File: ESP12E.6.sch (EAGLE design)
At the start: 63 parts, among them CN2 1X4-BIG, J1 1X2-3.5MM, J4 1X2-3.5MM, U1 A5984

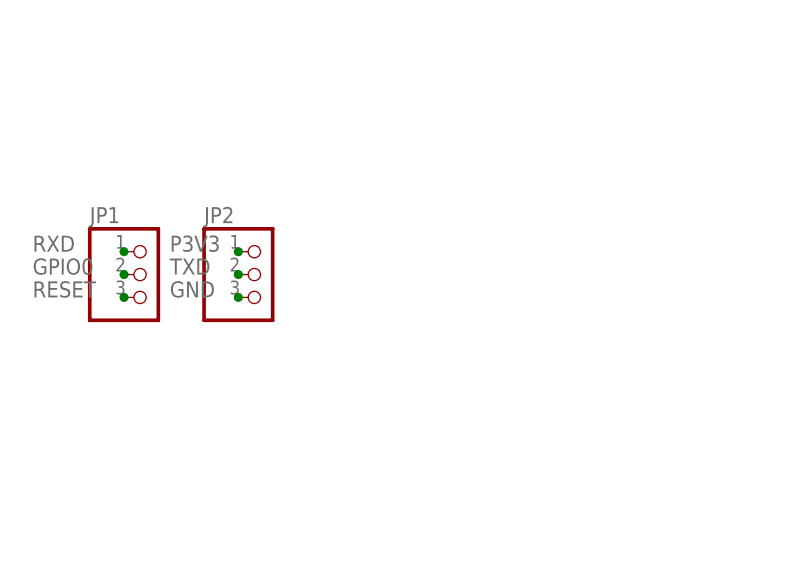
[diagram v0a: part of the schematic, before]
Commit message: //Lowered power via hole sizes to 18 AWG // Added ADC pin exposure
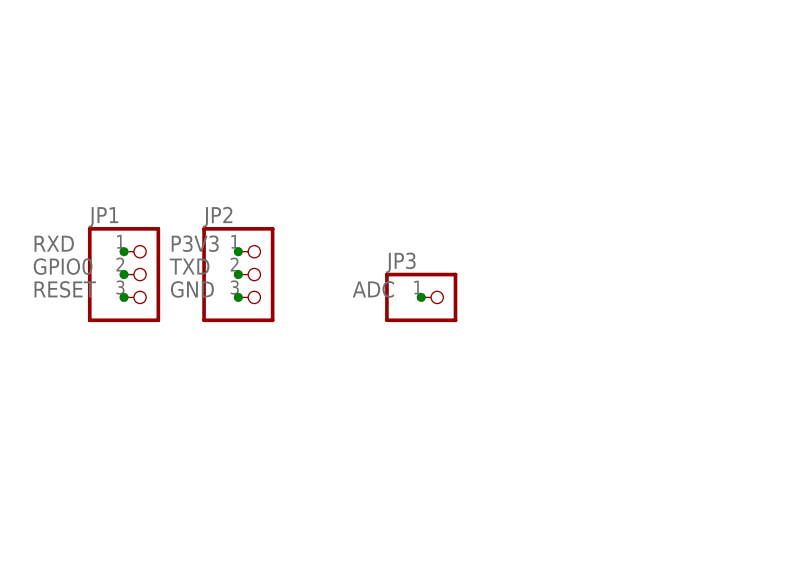
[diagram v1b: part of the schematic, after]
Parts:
- added JP3: (no value), adafruit:PINHD-1X1CB
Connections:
- net ADC: now also JP3.1
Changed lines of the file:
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@@
 <?xml version="1.0" encoding="utf-8"?>
 <!DOCTYPE eagle SYSTEM "eagle.dtd">
-<eagle version="7.2.0">
+<eagle version="8.3.1">
 <drawing>
 <settings>
 <setting alwaysvectorfont="no"/>
+<setting keepoldvectorfont="yes"/>
 <setting verticaltext="up"/>
 </settings>
@@
 <part name="TP2" library="testpad" deviceset="PTR1" device="B1,27"/>
 <part name="TP3" library="testpad" deviceset="PTR1" device="B1,27"/>
+<part name="JP3" library="adafruit" library_urn="urn:adsk.eagle:library:420" deviceset="PINHD-1X1" device="CB"/>
 </parts>
 <sheets>
@@
 <instance part="TP2" gate="G$1" x="401.32" y="254" rot="R180"/>
 <instance part="TP3" gate="G$1" x="297.18" y="200.66" rot="R180"/>
+<instance part="JP3" gate="G$1" x="63.5" y="154.94"/>
 </instances>
 <busses>
@@
 <label x="195.58" y="243.84" size="1.778" layer="95"/>
 </segment>
+<segment>
+<pinref part="JP3" gate="G$1" pin="1"/>
+<junction x="60.96" y="154.94"/>
+<label x="53.34" y="154.94" size="1.778" layer="95"/>
+</segment>
 </net>
 <net name="RESET" class="0">
@@
 which will not be processed correctly with this version.
 </note>
+<note version="8.2" severity="warning">
+Since Version 8.2, EAGLE supports online libraries. The ids
+of those online libraries will not be understood (or retained)
+with this version.
+</note>
 </compatibility>

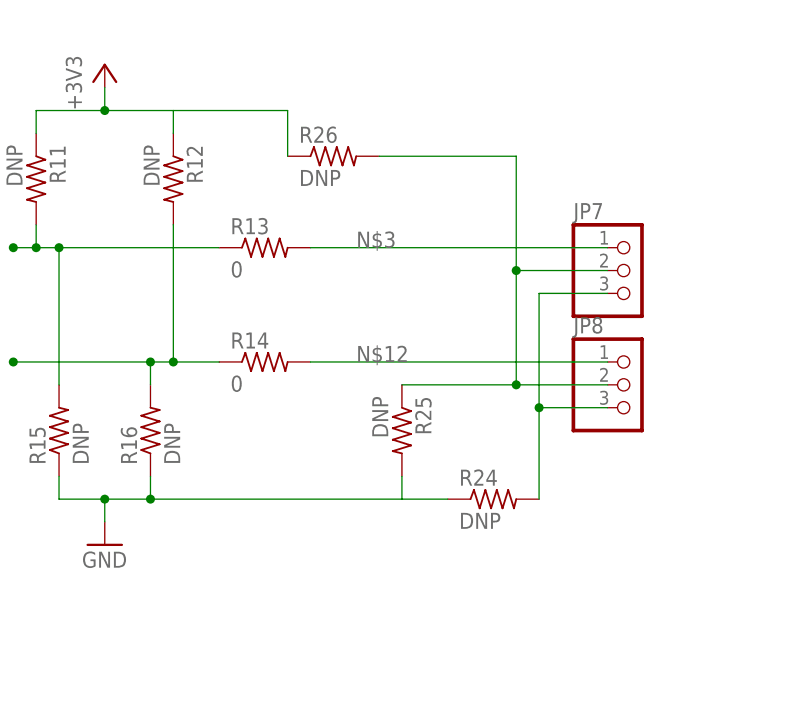
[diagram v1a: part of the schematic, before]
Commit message: Oct Update
Power drill size change and placment of IO pin resistors
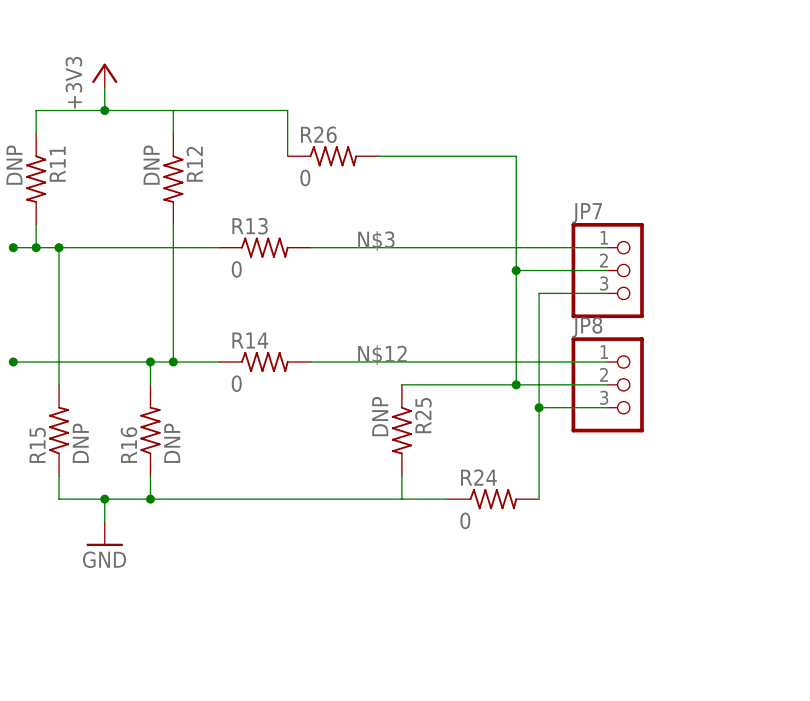
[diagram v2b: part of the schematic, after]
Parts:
- R24, R26: value DNP -> 0
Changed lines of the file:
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@@
 <part name="GND14" library="supply1" deviceset="GND" device=""/>
 <part name="+3V11" library="supply1" deviceset="+3V3" device=""/>
-<part name="R24" library="adafruit" deviceset="R-US_" device="R0603" value="DNP"/>
+<part name="R24" library="adafruit" deviceset="R-US_" device="R0603" value="0"/>
 <part name="JP7" library="adafruit" deviceset="PINHD-1X3" device=""/>
 <part name="JP8" library="adafruit" deviceset="PINHD-1X3" device=""/>
 <part name="R25" library="adafruit" deviceset="R-US_" device="R0603" value="DNP"/>
-<part name="R26" library="adafruit" deviceset="R-US_" device="R0603" value="DNP"/>
+<part name="R26" library="adafruit" deviceset="R-US_" device="R0603" value="0"/>
 <part name="U$2" library="TPS62177" deviceset="GRM21BR60J226ME39L" device=""/>
 <part name="U$3" library="TPS62177" deviceset="GRM188R61C225KE15D" device=""/>

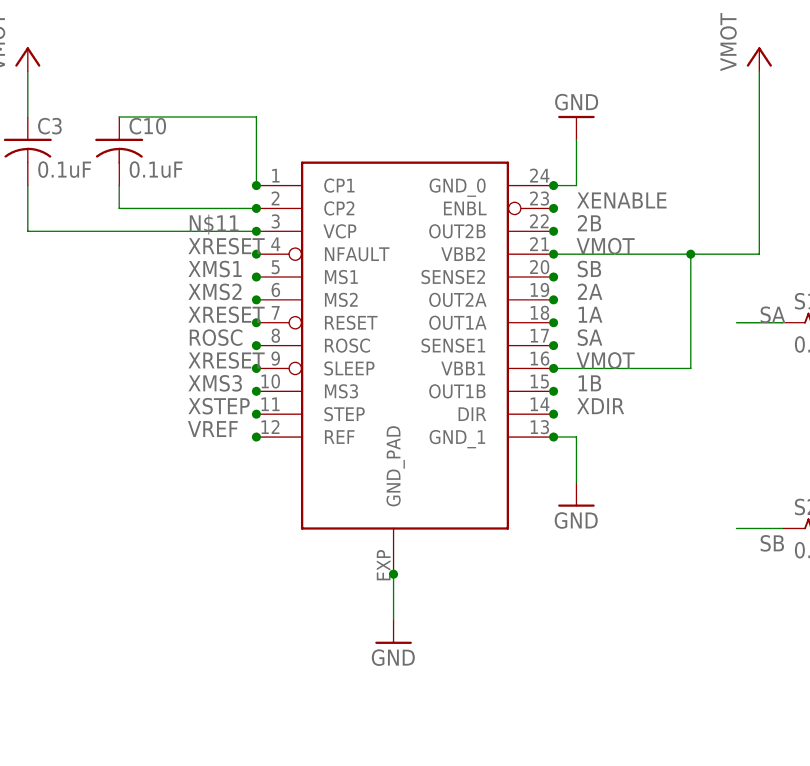
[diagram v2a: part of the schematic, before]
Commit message: A5984 QFN24
Layout with QFN24 driver
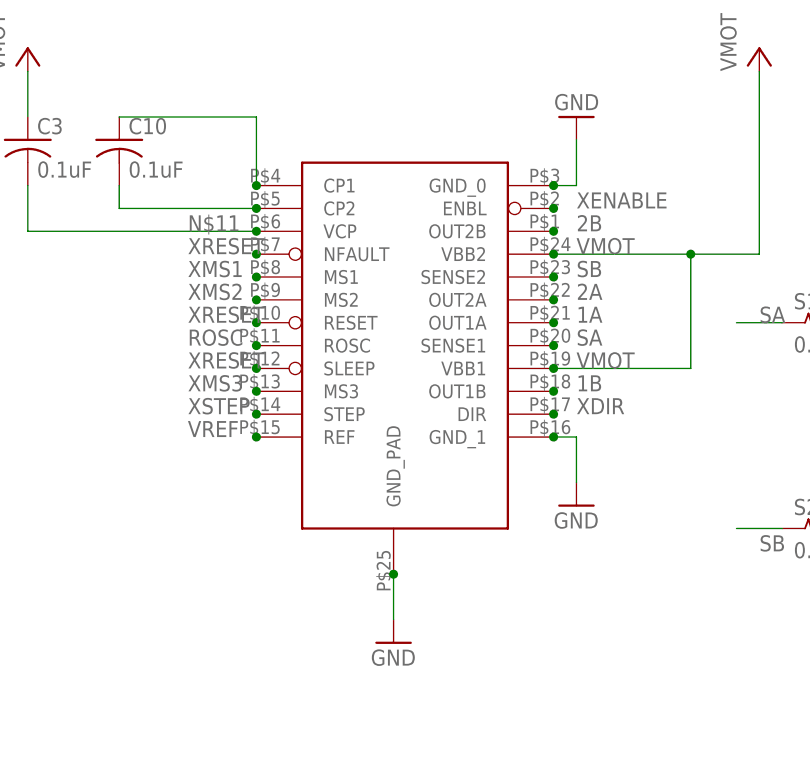
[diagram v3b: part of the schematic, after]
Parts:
- U1: device A5984:A5984-TSSOP -> A5984:A5984-24QFN
